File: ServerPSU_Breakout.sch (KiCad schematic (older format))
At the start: 0 parts

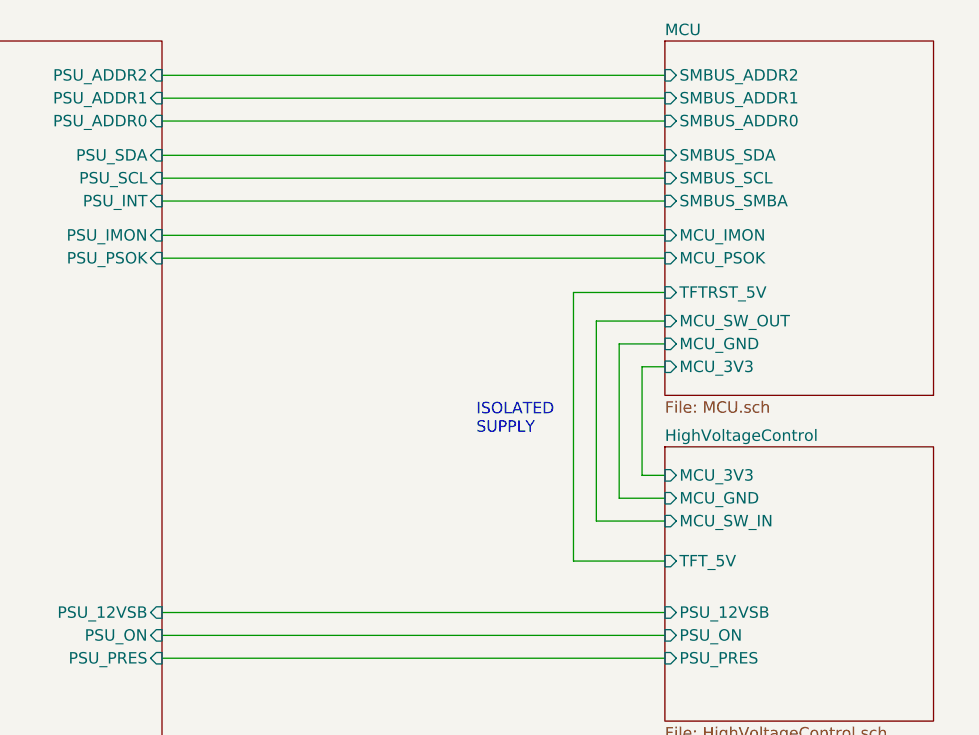
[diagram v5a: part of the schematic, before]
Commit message: updated hw
- added SMBUS address HW 
- Changed Isolated DC Module to TI SimpleSwitcher IC
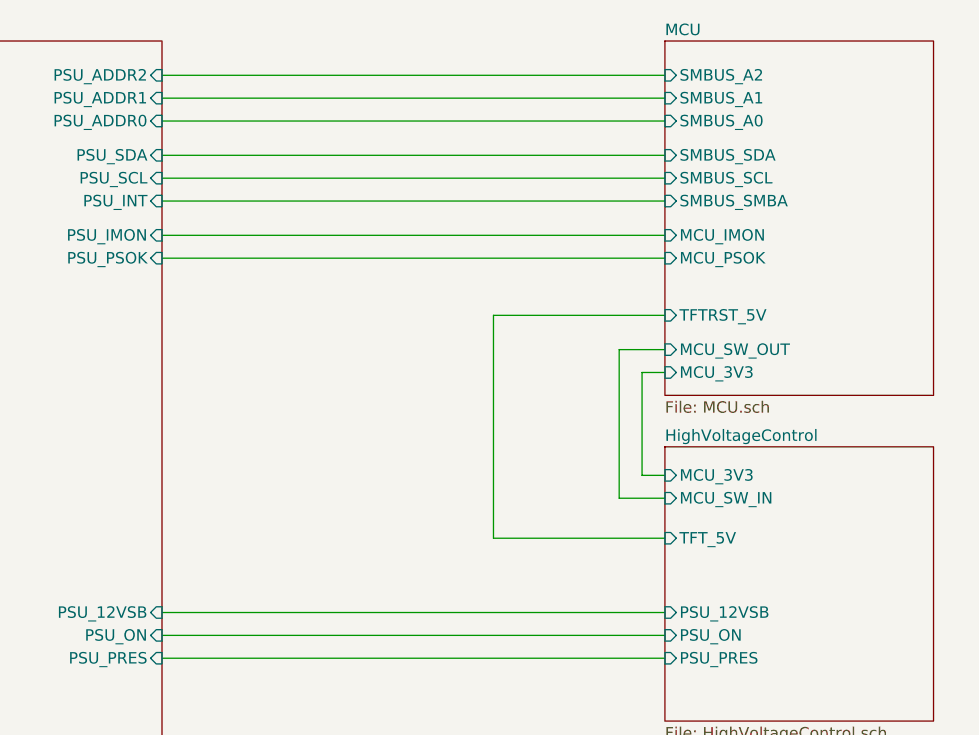
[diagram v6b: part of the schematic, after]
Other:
- note removed: "ISOLATED\nSUPPLY"
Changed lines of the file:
@@
 $Descr A4 8268 11693 portrait
 encoding utf-8
-Sheet 1 6
+Sheet 1 7
 Title ""
 Date "2020-06-30"
@@
 Wire Wire Line
 	5250 6300 3050 6300
-Text Notes 4425 4675 0    50   ~ 0
-ISOLATED\nSUPPLY
-Wire Wire Line
-	5250 3300 3050 3300
-Wire Wire Line
-	5250 3200 3050 3200
-Wire Wire Line
-	5250 3100 3050 3100
 $Sheet
 S 5250 2950 1175 1550
@@
 F0 "MCU" 50
 F1 "MCU.sch" 50
-F2 "MCU_GND" I L 5250 4275 50
-F3 "MCU_3V3" I L 5250 4375 50
-F4 "MCU_PSOK" I L 5250 3900 50
-F5 "SMBUS_SDA" I L 5250 3450 50
-F6 "SMBUS_SCL" I L 5250 3550 50
-F7 "SMBUS_SMBA" I L 5250 3650 50
-F8 "SMBUS_ADDR0" I L 5250 3300 50
-F9 "SMBUS_ADDR1" I L 5250 3200 50
-F10 "SMBUS_ADDR2" I L 5250 3100 50
-F11 "MCU_IMON" I L 5250 3800 50
-F12 "TFTRST_5V" I L 5250 4050 50
-F13 "MCU_SW_OUT" I L 5250 4175 50
+F2 "MCU_3V3" I L 5250 4400 50
+F3 "MCU_PSOK" I L 5250 3900 50
+F4 "SMBUS_SDA" I L 5250 3450 50
+F5 "SMBUS_SCL" I L 5250 3550 50
+F6 "SMBUS_SMBA" I L 5250 3650 50
+F7 "MCU_IMON" I L 5250 3800 50
+F8 "TFTRST_5V" I L 5250 4150 50
+F9 "MCU_SW_OUT" I L 5250 4300 50
+F10 "SMBUS_A0" I L 5250 3300 50
+F11 "SMBUS_A1" I L 5250 3200 50
+F12 "SMBUS_A2" I L 5250 3100 50
 $EndSheet
 $Sheet
@@
 	5250 3900 3050 3900
 Wire Wire Line
-	5050 4275 5250 4275
+	5050 4300 5250 4300
 Wire Wire Line
-	4950 4175 5250 4175
+	5250 4400 5150 4400
 Wire Wire Line
-	5250 4375 5150 4375
-Wire Wire Line
-	5150 4375 5150 4850
+	5150 4400 5150 4850
 Wire Wire Line
 	5150 4850 5250 4850
 Wire Wire Line
-	5050 4950 5050 4275
+	5050 4950 5050 4300
 Wire Wire Line
 	5250 4950 5050 4950
-Wire Wire Line
-	4950 5050 4950 4175
-Wire Wire Line
-	5250 5050 4950 5050
 $Sheet
 S 5250 4725 1175 1200
@@
 F1 "HighVoltageControl.sch" 50
 F2 "PSU_12VSB" I L 5250 5450 50
-F3 "MCU_GND" I L 5250 4950 50
-F4 "MCU_3V3" I L 5250 4850 50
-F5 "PSU_ON" I L 5250 5550 50
-F6 "PSU_PRES" I L 5250 5650 50
-F7 "MCU_SW_IN" I L 5250 5050 50
-F8 "TFT_5V" I L 5250 5225 50
+F3 "MCU_3V3" I L 5250 4850 50
+F4 "PSU_ON" I L 5250 5550 50
+F5 "PSU_PRES" I L 5250 5650 50
+F6 "MCU_SW_IN" I L 5250 4950 50
+F7 "TFT_5V" I L 5250 5125 50
 $EndSheet
 Wire Wire Line
-	5250 4050 4850 4050
+	5250 4150 4500 4150
 Wire Wire Line
-	4850 4050 4850 5225
+	4500 4150 4500 5125
 Wire Wire Line
-	4850 5225 5250 5225
+	4500 5125 5250 5125
+Wire Wire Line
+	5250 3300 3050 3300
+Wire Wire Line
+	3050 3200 5250 3200
+Wire Wire Line
+	3050 3100 5250 3100
 $EndSCHEMATC
